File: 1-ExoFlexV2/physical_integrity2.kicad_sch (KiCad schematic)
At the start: 23 parts, among them U74 SN74LVC1G32DBVR, U75 SN74LVC1G32DBVR, U76 SN74LVC1G32DBVR, U77 SN74LVC1G32DBVR, U79 SN74LVC1G32DBVR

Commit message: Schématisation terminée
- Schéma terminé
- Passage vers le PCB
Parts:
- J117, J118, J119, J120, J121, J122: renamed from J?; value Jmp -> Jumper; footprint (none) -> Connector_PinSocket_2.54mm:PinSocket_1x03_P2.54mm_Vertical; DESCRIPTION (none) -> CONN HEADER VERT 3POS 2.54MM; MANUFACTURER (none) -> Würth Elektronik; PACKAGE (none) -> Square 0.100" (2.54mm); PART NUMBER (none) -> 61300311121; TYPE (none) -> Through Hole
- R182, R183, R184, R185, R186, R187, R188, R189, R190, R191, R192, R193: renamed from R?; value 100k -> 100k 5% 1/8W; DESCRIPTION (none) -> 100 kOhms ±5% 0.125W, 1/8W Chip Resistor 0805 (2012 Metric)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; MANUFACTURER (none) -> Panasonic Electronic Components; PACKAGE (none) -> 0805 (2012 Metric); PART NUMBER (none) -> ERJ-6GEYJ104V; TYPE (none) -> SMD
- U93: renamed from U74; value SN74LVC1G32DBVR -> OR Gate; DESCRIPTION (none) -> OR Gate IC 1 Channel SOT-23-5; MANUFACTURER (none) -> Texas Instruments; PACKAGE (none) -> SC-74A, SOT-753; PART NUMBER (none) -> SN74LVC1G32DBVR; TYPE (none) -> SMD
- U94: renamed from U75; value SN74LVC1G32DBVR -> OR Gate; DESCRIPTION (none) -> OR Gate IC 1 Channel SOT-23-5; MANUFACTURER (none) -> Texas Instruments; PACKAGE (none) -> SC-74A, SOT-753; PART NUMBER (none) -> SN74LVC1G32DBVR; TYPE (none) -> SMD
- U95: renamed from U76; value SN74LVC1G32DBVR -> OR Gate; DESCRIPTION (none) -> OR Gate IC 1 Channel SOT-23-5; MANUFACTURER (none) -> Texas Instruments; PACKAGE (none) -> SC-74A, SOT-753; PART NUMBER (none) -> SN74LVC1G32DBVR; TYPE (none) -> SMD
- U96: renamed from U77; value SN74LVC1G32DBVR -> OR Gate; DESCRIPTION (none) -> OR Gate IC 1 Channel SOT-23-5; MANUFACTURER (none) -> Texas Instruments; PACKAGE (none) -> SC-74A, SOT-753; PART NUMBER (none) -> SN74LVC1G32DBVR; TYPE (none) -> SMD
- U97: renamed from U79; value SN74LVC1G32DBVR -> OR Gate; DESCRIPTION (none) -> OR Gate IC 1 Channel SOT-23-5; MANUFACTURER (none) -> Texas Instruments; PACKAGE (none) -> SC-74A, SOT-753; PART NUMBER (none) -> SN74LVC1G32DBVR; TYPE (none) -> SMD
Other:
- note added: "5xORGate : 5V @ 160,05mA 12x100k : 5V @ 0,6mA Total current : 5V @ 165mA"
- note removed: "5xORGate : 5V @ 160,05mA 6x100k : 5V @ 0,3mA 6x200k : 5V @ 0,15mA Total current : 5V @ 162mA"
- moved on the sheet: J117, J118, J119, J120, J121, J122, R182, R183, R184, R185, R186, R187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

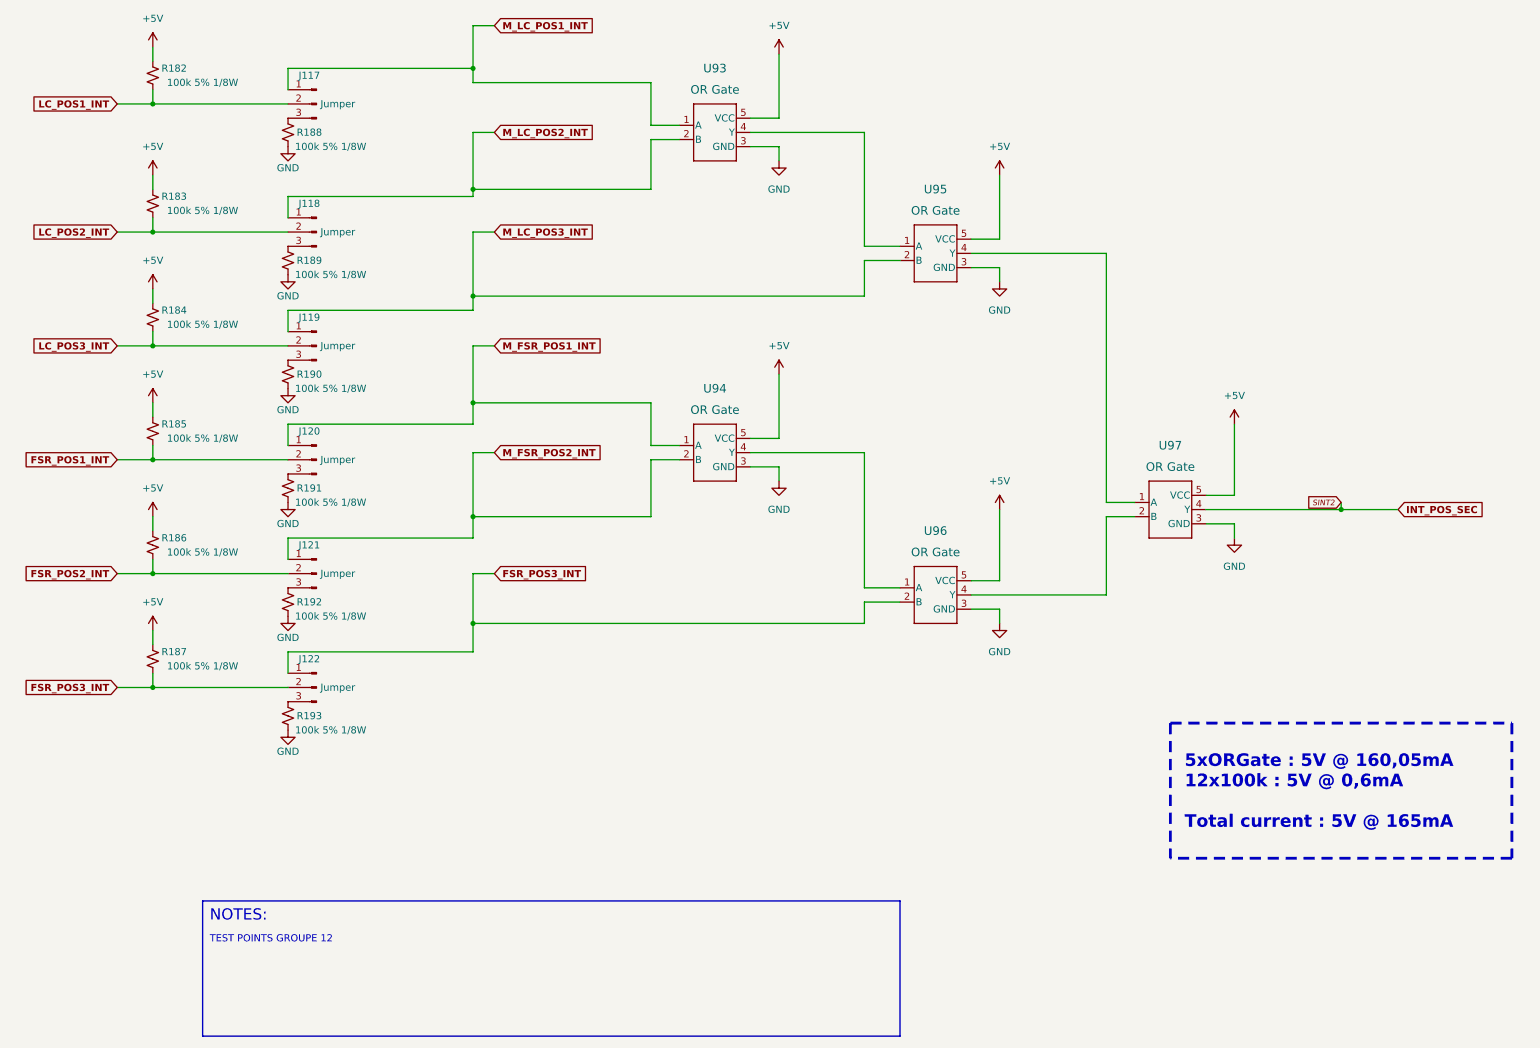
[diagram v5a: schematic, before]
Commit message: Finalisation 3
- Changement des régulateur de tension
- Retrait de test point inutile
- Changement de jumper mal positionner
- Ajout de Mounting holes et fiducial
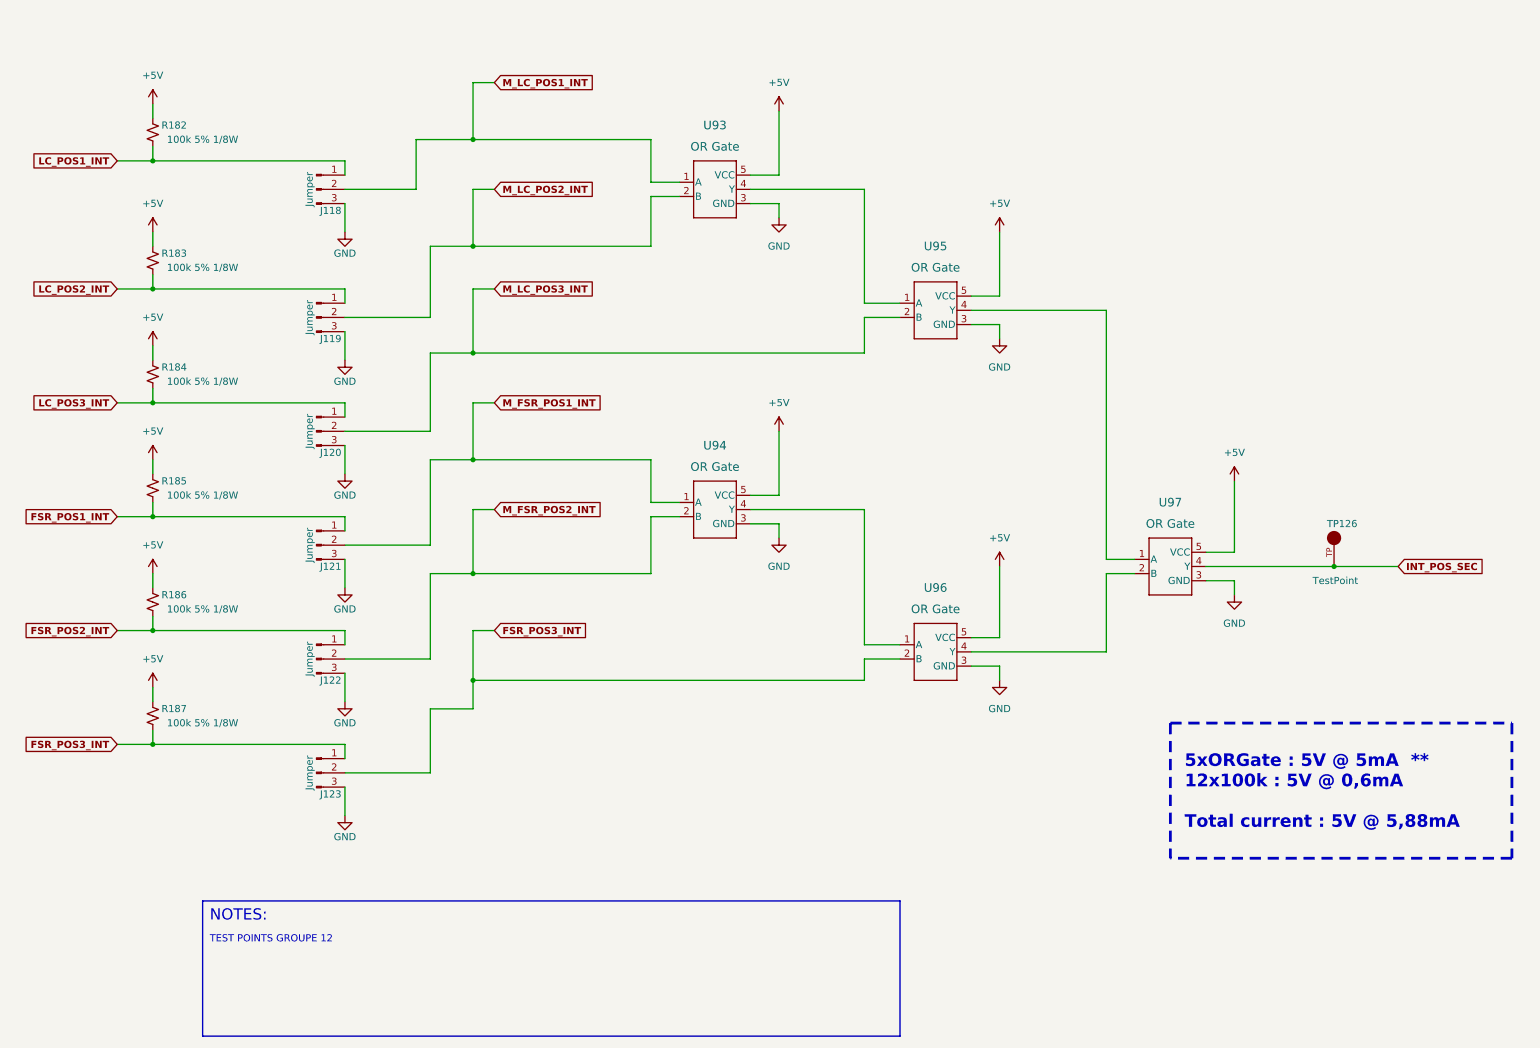
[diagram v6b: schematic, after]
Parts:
- removed R188, R189, R190, R191, R192, R193: 100k 5% 1/8W, Resistor_SMD:R_0805_2012Metric, symbol Device:R_Small_US
- added TP126: TestPoint, FootPrint:KEYSTONE_5005, symbol SymLib:5005
- J118: renamed from J117; footprint Connector_PinSocket_2.54mm:PinSocket_1x03_P2.54mm_Vertical -> Connector_PinHeader_2.54mm:PinHeader_1x03_P2.54mm_Vertical
- J119: renamed from J118; footprint Connector_PinSocket_2.54mm:PinSocket_1x03_P2.54mm_Vertical -> Connector_PinHeader_2.54mm:PinHeader_1x03_P2.54mm_Vertical
- J120: renamed from J119; footprint Connector_PinSocket_2.54mm:PinSocket_1x03_P2.54mm_Vertical -> Connector_PinHeader_2.54mm:PinHeader_1x03_P2.54mm_Vertical
- J121: renamed from J120; footprint Connector_PinSocket_2.54mm:PinSocket_1x03_P2.54mm_Vertical -> Connector_PinHeader_2.54mm:PinHeader_1x03_P2.54mm_Vertical
- J122: renamed from J121; footprint Connector_PinSocket_2.54mm:PinSocket_1x03_P2.54mm_Vertical -> Connector_PinHeader_2.54mm:PinHeader_1x03_P2.54mm_Vertical
- J123: renamed from J122; footprint Connector_PinSocket_2.54mm:PinSocket_1x03_P2.54mm_Vertical -> Connector_PinHeader_2.54mm:PinHeader_1x03_P2.54mm_Vertical
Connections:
- net FSR_POS1_INT: now also J121.1 (Pin_1); no longer J121.2 (Pin_2)
- net FSR_POS2_INT: now also J122.1 (Pin_1); no longer J122.2 (Pin_2)
- net GND: now also J118.3 (Pin_3), J119.3 (Pin_3), J120.3 (Pin_3), J121.3 (Pin_3), J122.3 (Pin_3), J123.3 (Pin_3)
- net INT_POS_SEC: now also TP126.TP
- net LC_POS1_INT: now also J118.1 (Pin_1); no longer J118.2 (Pin_2)
- net LC_POS2_INT: now also J119.1 (Pin_1); no longer J119.2 (Pin_2)
- net LC_POS3_INT: now also J120.1 (Pin_1); no longer J120.2 (Pin_2)
- net M_FSR_POS1_INT: now also J121.2 (Pin_2); no longer J121.1 (Pin_1)
- net M_FSR_POS2_INT: now also J122.2 (Pin_2); no longer J122.1 (Pin_1)
- net M_LC_POS1_INT: now also J118.2 (Pin_2); no longer J118.1 (Pin_1)
- net M_LC_POS2_INT: now also J119.2 (Pin_2); no longer J119.1 (Pin_1)
- net M_LC_POS3_INT: now also J120.2 (Pin_2); no longer J120.1 (Pin_1)
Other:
- note added: "5xORGate : 5V @ 5mA ** 12x100k : 5V @ 0,6mA Total current : 5V @ 5,88mA"
- note removed: "5xORGate : 5V @ 160,05mA 12x100k : 5V @ 0,6mA Total current : 5V @ 165mA"
- moved on the sheet: J118, J119, J120, J121, J122, J123, R182, R183, R184, R185, R186, R187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

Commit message: Finalisation schéma FIN
- Changement des uméro pour les inverseurs
- Changement des connecteur et début de placement
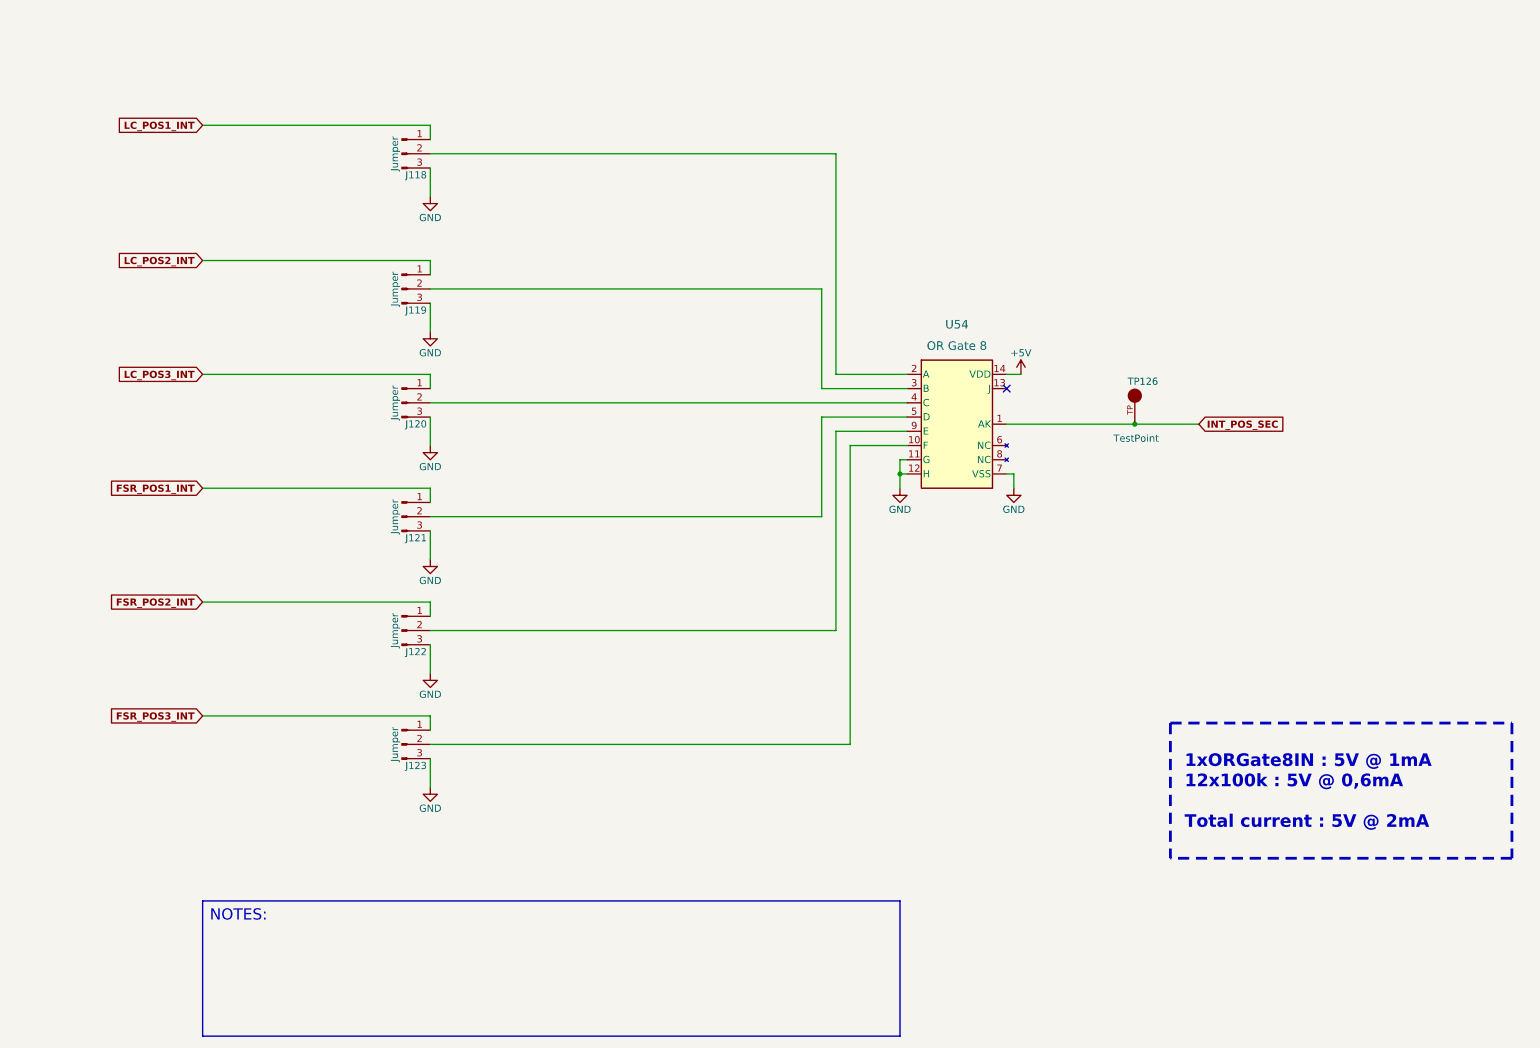
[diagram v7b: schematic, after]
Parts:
- removed R182, R183, R184, R185, R186, R187: 100k 5% 1/8W, Resistor_SMD:R_0805_2012Metric, symbol Device:R_Small_US
- removed U93, U94, U95, U96, U97: OR Gate, FootPrint:SOT95P270X145-5N, symbol SymLib:SN74LVC1G32DBVR
- added U54: OR Gate 8, FootPrint:D14, symbol SymLib:CD4078BM96
- TP126: NOTES (none) -> DO NOT POPULATE; PURCHASE-URL https://pricing.snapeda.com/search/part/5005/?ref=eda -> (none)
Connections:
- net +5V: now also U54.14 (VDD)
- net FSR_POS3_INT: no longer J123.2 (Pin_2)
- net GND: now also U54.11 (G), U54.12 (H), U54.7 (VSS)
- net INT_POS_SEC: now also U54.1 (AK)
- net M_FSR_POS1_INT: no longer names the net of J121.2 (Pin_2)
- net M_FSR_POS1_INT: now also U54.5 (D)
- net M_FSR_POS2_INT: no longer names the net of J122.2 (Pin_2)
- net M_FSR_POS2_INT: now also U54.9 (E)
- net M_LC_POS1_INT: no longer names the net of J118.2 (Pin_2)
- net M_LC_POS1_INT: now also U54.2 (A)
- net M_LC_POS2_INT: no longer names the net of J119.2 (Pin_2)
- net M_LC_POS2_INT: now also U54.3 (B)
- net M_LC_POS3_INT: no longer names the net of J120.2 (Pin_2)
- net M_LC_POS3_INT: now also U54.4 (C)
- new net: J123.2 (Pin_2), U54.10 (F)
- no-connect marks 0 -> 1
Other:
- note added: "1xORGate8IN : 5V @ 1mA 12x100k : 5V @ 0,6mA Total current : 5V @ 2mA"
- note removed: "5xORGate : 5V @ 5mA ** 12x100k : 5V @ 0,6mA Total current : 5V @ 5,88mA"
- note removed: "TEST POINTS GROUPE 12"
- moved on the sheet: J118, J119, J120, J121, J122, J123, TP126

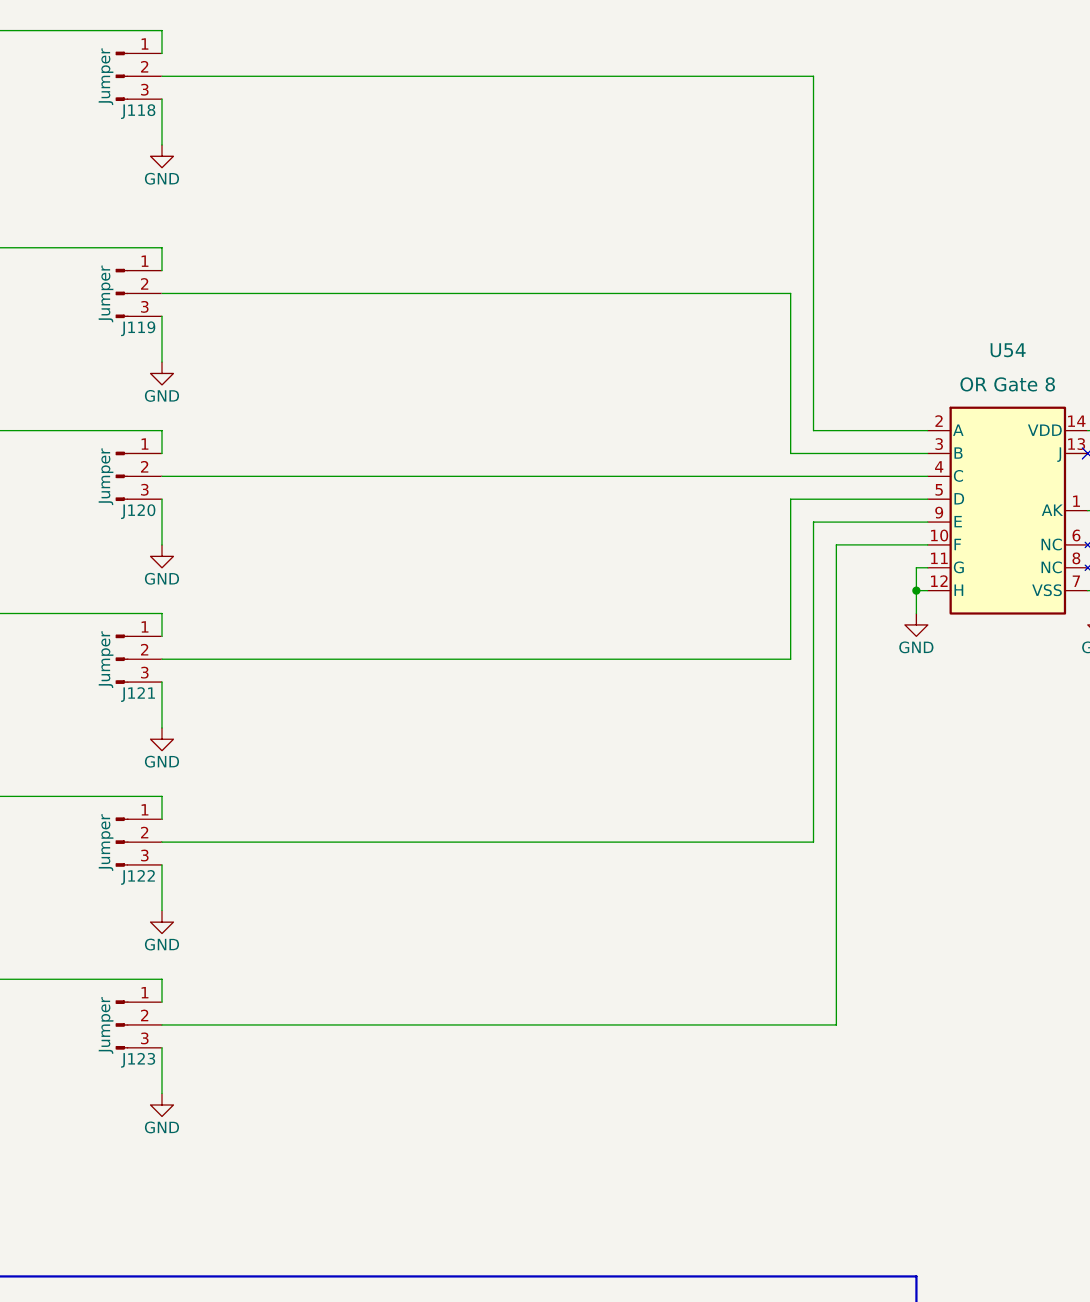
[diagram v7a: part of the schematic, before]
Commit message: Routage pour Review 1
- Replacement des test point pour faciliter le rework
- Correction des erreurs dans le BOM
-
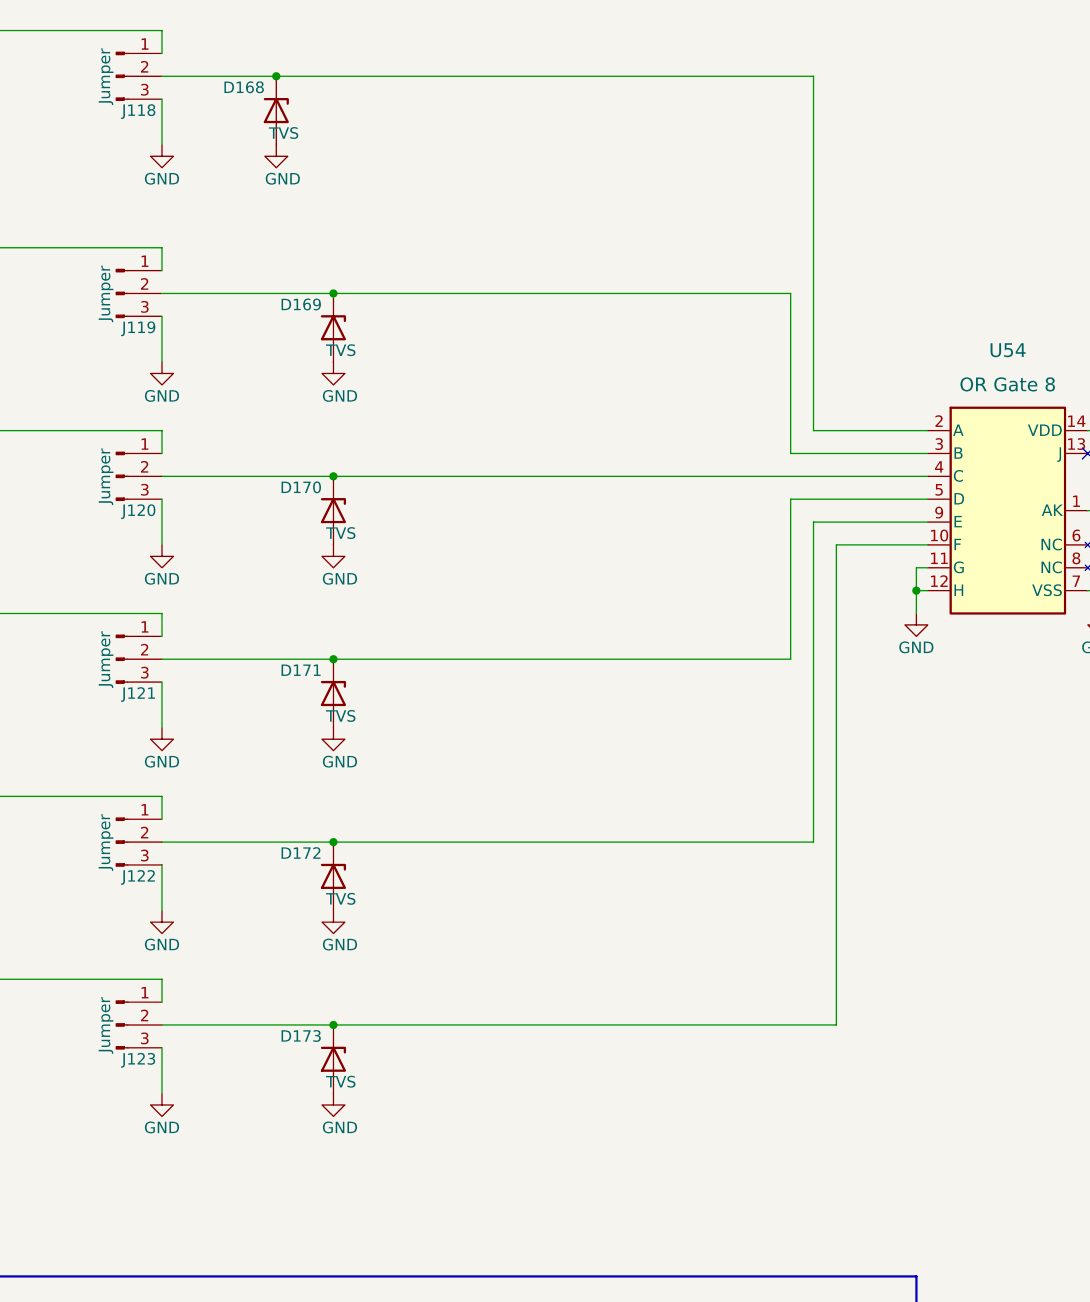
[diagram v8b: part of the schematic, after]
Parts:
- added D168, D169, D170, D171, D172, D173: TVS, FootPrint:DPY2_TEX, symbol Device:D_Zener
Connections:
- net GND: now also D168.2 (A), D169.2 (A), D170.2 (A), D171.2 (A), D172.2 (A), D173.2 (A)
- net at J121.2 (Pin_2), U54.5 (D): now also D171.1 (K)
- net at J123.2 (Pin_2), U54.10 (F): now also D173.1 (K)
- net at J118.2 (Pin_2), U54.2 (A): now also D168.1 (K)
- net at J119.2 (Pin_2), U54.3 (B): now also D169.1 (K)
- net at J120.2 (Pin_2), U54.4 (C): now also D170.1 (K)
- net at J122.2 (Pin_2), U54.9 (E): now also D172.1 (K)
